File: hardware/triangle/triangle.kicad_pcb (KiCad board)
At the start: 4 copper layers, 100 x 86.6 mm, 70 parts, among them J1 USB_C_Receptacle_USB2.0_16P, J2 USB_C_Receptacle_USB2.0_16P, U2 EA8212HT6R

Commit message: rearranging shared files and input board beginnings
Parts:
- D1, D10, D11, D12, D13, D14, D15, D16, D17, D18, D19, D2, D20, D21, D22, D23, D24, D3, D4, D5, D6, D7, D8, D9: footprint footprints:LED_WS2812B-2020_PLCC4_2.0x2.0mm - no silkscreen -> easyeda2kicad:LED_WS2812B-2020_PLCC4_2.0x2.0mm - no silkscreen
- J1, J2: footprint footprints:TYPE-C-SMD_USB4120-03-C -> easyeda2kicad:TYPE-C-SMD_USB4120-03-C
- U2: footprint footprints:SOT-23-6_L2.9-W1.6-P0.95-LS2.8-BR -> easyeda2kicad:SOT-23-6_L2.9-W1.6-P0.95-LS2.8-BR
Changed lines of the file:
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@@
 		(embedded_fonts no)
 	)
-	(footprint "footprints:LED_WS2812B-2020_PLCC4_2.0x2.0mm - no silkscreen"
+	(footprint "easyeda2kicad:LED_WS2812B-2020_PLCC4_2.0x2.0mm - no silkscreen"
 		(layer "F.Cu")
 		(at 150 145 180)
@@
 		)
 	)
-	(footprint "footprints:LED_WS2812B-2020_PLCC4_2.0x2.0mm - no silkscreen"
+	(footprint "easyeda2kicad:LED_WS2812B-2020_PLCC4_2.0x2.0mm - no silkscreen"
 		(layer "F.Cu")
 		(at 165.5025 100.248125 -60)
@@
 		)
 	)
-	(footprint "footprints:LED_WS2812B-2020_PLCC4_2.0x2.0mm - no silkscreen"
+	(footprint "easyeda2kicad:LED_WS2812B-2020_PLCC4_2.0x2.0mm - no silkscreen"
 		(layer "F.Cu")
 		(at 189.02 143.84 -120)
@@
 		)
 	)
-	(footprint "footprints:LED_WS2812B-2020_PLCC4_2.0x2.0mm - no silkscreen"
+	(footprint "easyeda2kicad:LED_WS2812B-2020_PLCC4_2.0x2.0mm - no silkscreen"
 		(layer "F.Cu")
 		(at 118.995 127.09925 60)
@@
 		)
 	)
-	(footprint "footprints:LED_WS2812B-2020_PLCC4_2.0x2.0mm - no silkscreen"
+	(footprint "easyeda2kicad:LED_WS2812B-2020_PLCC4_2.0x2.0mm - no silkscreen"
 		(layer "F.Cu")
 		(at 160.335 145 180)
@@
 		)
 	)
-	(footprint "footprints:LED_WS2812B-2020_PLCC4_2.0x2.0mm - no silkscreen"
+	(footprint "easyeda2kicad:LED_WS2812B-2020_PLCC4_2.0x2.0mm - no silkscreen"
 		(layer "F.Cu")
 		(at 124.1625 118.148875 60)
@@
 		)
 	)
-	(footprint "footprints:LED_WS2812B-2020_PLCC4_2.0x2.0mm - no silkscreen"
+	(footprint "easyeda2kicad:LED_WS2812B-2020_PLCC4_2.0x2.0mm - no silkscreen"
 		(layer "F.Cu")
 		(at 186.1725 136.049625 -60)
@@
 		)
 	)
-	(footprint "footprints:LED_WS2812B-2020_PLCC4_2.0x2.0mm - no silkscreen"
+	(footprint "easyeda2kicad:LED_WS2812B-2020_PLCC4_2.0x2.0mm - no silkscreen"
 		(layer "F.Cu")
 		(at 139.665 91.29775 60)
@@
 		)
 	)
-	(footprint "footprints:LED_WS2812B-2020_PLCC4_2.0x2.0mm - no silkscreen"
+	(footprint "easyeda2kicad:LED_WS2812B-2020_PLCC4_2.0x2.0mm - no silkscreen"
 		(layer "F.Cu")
 		(at 134.4975 100.248125 60)
@@
 		)
 	)
-	(footprint "footprints:LED_WS2812B-2020_PLCC4_2.0x2.0mm - no silkscreen"
+	(footprint "easyeda2kicad:LED_WS2812B-2020_PLCC4_2.0x2.0mm - no silkscreen"
 		(layer "F.Cu")
 		(at 160.335 91.29775 -60)
@@
 		)
 	)
-	(footprint "footprints:LED_WS2812B-2020_PLCC4_2.0x2.0mm - no silkscreen"
+	(footprint "easyeda2kicad:LED_WS2812B-2020_PLCC4_2.0x2.0mm - no silkscreen"
 		(layer "F.Cu")
 		(at 144.8325 82.347375 60)
@@
 		)
 	)
-	(footprint "footprints:LED_WS2812B-2020_PLCC4_2.0x2.0mm - no silkscreen"
+	(footprint "easyeda2kicad:LED_WS2812B-2020_PLCC4_2.0x2.0mm - no silkscreen"
 		(layer "F.Cu")
 		(at 129.329999 145 180)
@@
 		(embedded_fonts no)
 	)
-	(footprint "footprints:LED_WS2812B-2020_PLCC4_2.0x2.0mm - no silkscreen"
+	(footprint "easyeda2kicad:LED_WS2812B-2020_PLCC4_2.0x2.0mm - no silkscreen"
 		(layer "F.Cu")
 		(at 110.825639 143.598161 120)
@@
 		)
 	)
-	(footprint "footprints:LED_WS2812B-2020_PLCC4_2.0x2.0mm - no silkscreen"
+	(footprint "easyeda2kicad:LED_WS2812B-2020_PLCC4_2.0x2.0mm - no silkscreen"
 		(layer "F.Cu")
 		(at 175.8375 118.148875 -60)
@@
 		)
 	)
-	(footprint "footprints:LED_WS2812B-2020_PLCC4_2.0x2.0mm - no silkscreen"
+	(footprint "easyeda2kicad:LED_WS2812B-2020_PLCC4_2.0x2.0mm - no silkscreen"
 		(layer "F.Cu")
 		(at 181.005 145 180)
@@
 		)
 	)
-	(footprint "footprints:LED_WS2812B-2020_PLCC4_2.0x2.0mm - no silkscreen"
+	(footprint "easyeda2kicad:LED_WS2812B-2020_PLCC4_2.0x2.0mm - no silkscreen"
 		(layer "F.Cu")
 		(at 170.67 145 180)
@@
 		)
 	)
-	(footprint "footprints:LED_WS2812B-2020_PLCC4_2.0x2.0mm - no silkscreen"
+	(footprint "easyeda2kicad:LED_WS2812B-2020_PLCC4_2.0x2.0mm - no silkscreen"
 		(layer "F.Cu")
 		(at 129.329999 109.1985 60)
@@
 		)
 	)
-	(footprint "footprints:LED_WS2812B-2020_PLCC4_2.0x2.0mm - no silkscreen"
+	(footprint "easyeda2kicad:LED_WS2812B-2020_PLCC4_2.0x2.0mm - no silkscreen"
 		(layer "F.Cu")
 		(at 113.8275 136.049625 60)
@@
 		(embedded_fonts no)
 	)
-	(footprint "footprints:LED_WS2812B-2020_PLCC4_2.0x2.0mm - no silkscreen"
+	(footprint "easyeda2kicad:LED_WS2812B-2020_PLCC4_2.0x2.0mm - no silkscreen"
 		(layer "F.Cu")
 		(at 170.67 109.1985 -60)
@@
 		)
 	)
-	(footprint "footprints:LED_WS2812B-2020_PLCC4_2.0x2.0mm - no silkscreen"
+	(footprint "easyeda2kicad:LED_WS2812B-2020_PLCC4_2.0x2.0mm - no silkscreen"
 		(layer "F.Cu")
 		(at 155.1675 82.347375 -60)
@@
 		)
 	)
-	(footprint "footprints:LED_WS2812B-2020_PLCC4_2.0x2.0mm - no silkscreen"
+	(footprint "easyeda2kicad:LED_WS2812B-2020_PLCC4_2.0x2.0mm - no silkscreen"
 		(layer "F.Cu")
 		(at 181.005 127.09925 -60)
@@
 		)
 	)
-	(footprint "footprints:LED_WS2812B-2020_PLCC4_2.0x2.0mm - no silkscreen"
+	(footprint "easyeda2kicad:LED_WS2812B-2020_PLCC4_2.0x2.0mm - no silkscreen"
 		(layer "F.Cu")
 		(at 118.995 145 180)
@@
 		)
 	)
-	(footprint "footprints:LED_WS2812B-2020_PLCC4_2.0x2.0mm - no silkscreen"
+	(footprint "easyeda2kicad:LED_WS2812B-2020_PLCC4_2.0x2.0mm - no silkscreen"
 		(layer "F.Cu")
 		(at 150 75.397)
@@
 		)
 	)
-	(footprint "footprints:LED_WS2812B-2020_PLCC4_2.0x2.0mm - no silkscreen"
+	(footprint "easyeda2kicad:LED_WS2812B-2020_PLCC4_2.0x2.0mm - no silkscreen"
 		(layer "F.Cu")
 		(at 139.665 145 180)
@@
 		)
 	)
-	(footprint "footprints:TYPE-C-SMD_USB4120-03-C"
+	(footprint "easyeda2kicad:TYPE-C-SMD_USB4120-03-C"
 		(layer "B.Cu")
 		(at 133.345625 130.607088 -150)
@@
 		)
 	)
-	(footprint "footprints:TYPE-C-SMD_USB4120-03-C"
+	(footprint "easyeda2kicad:TYPE-C-SMD_USB4120-03-C"
 		(layer "B.Cu")
 		(at 149.896593 102.269695 90)
@@
 		)
 	)
-	(footprint "footprints:SOT-23-6_L2.9-W1.6-P0.95-LS2.8-BR"
+	(footprint "easyeda2kicad:SOT-23-6_L2.9-W1.6-P0.95-LS2.8-BR"
 		(layer "B.Cu")
 		(at 165.576901 117.879661 30)
@@
 		)
 		(embedded_fonts no)
-		(model "${EASYEDA2KICAD}/easyeda2kicad.3dshapes/SOT-23-6_L2.9-W1.6-H1.5-LS2.8-P0.95.wrl"
+		(model "${KIPRJMOD}/../shared/easyeda2kicad.3dshapes/SOT-23-6_L2.9-W1.6-H1.5-LS2.8-P0.95.wrl"
 			(offset
 				(xyz 0 0 0)

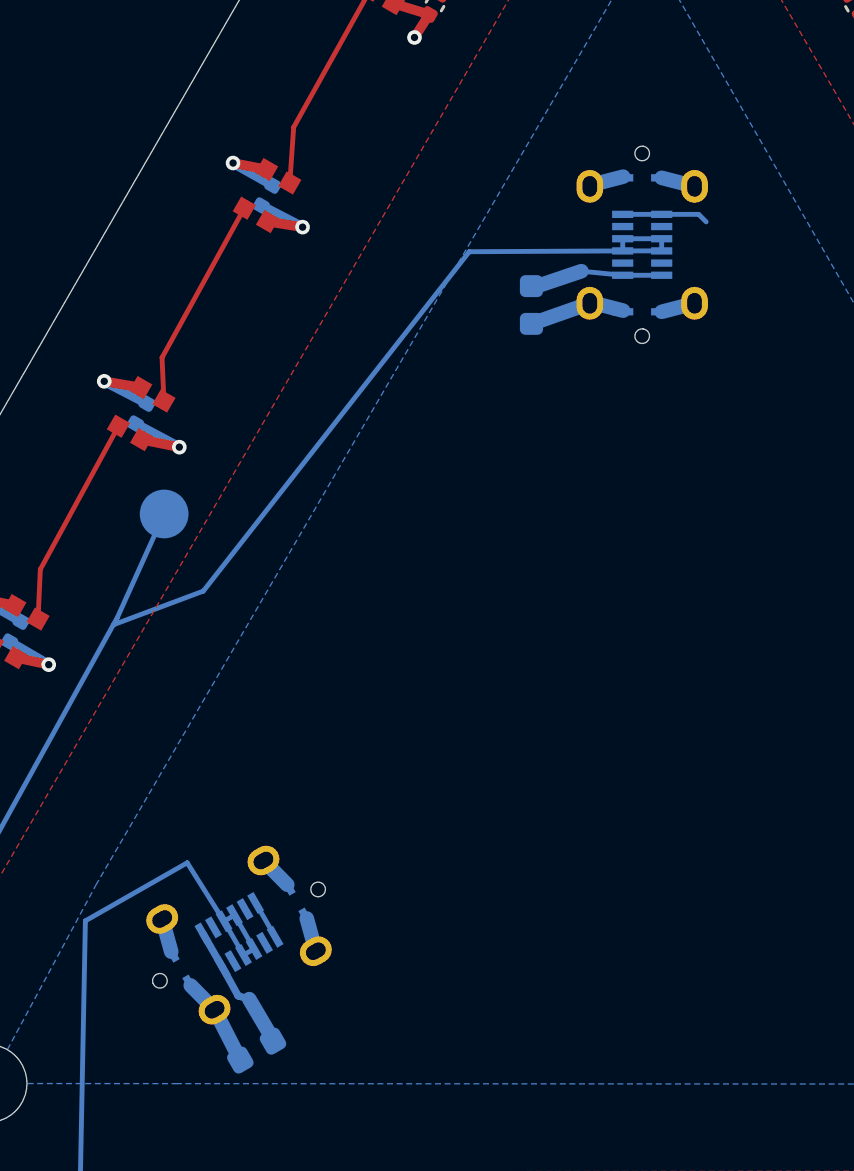
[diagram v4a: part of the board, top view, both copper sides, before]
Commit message: triangle rework to use new symbols and get all shapes
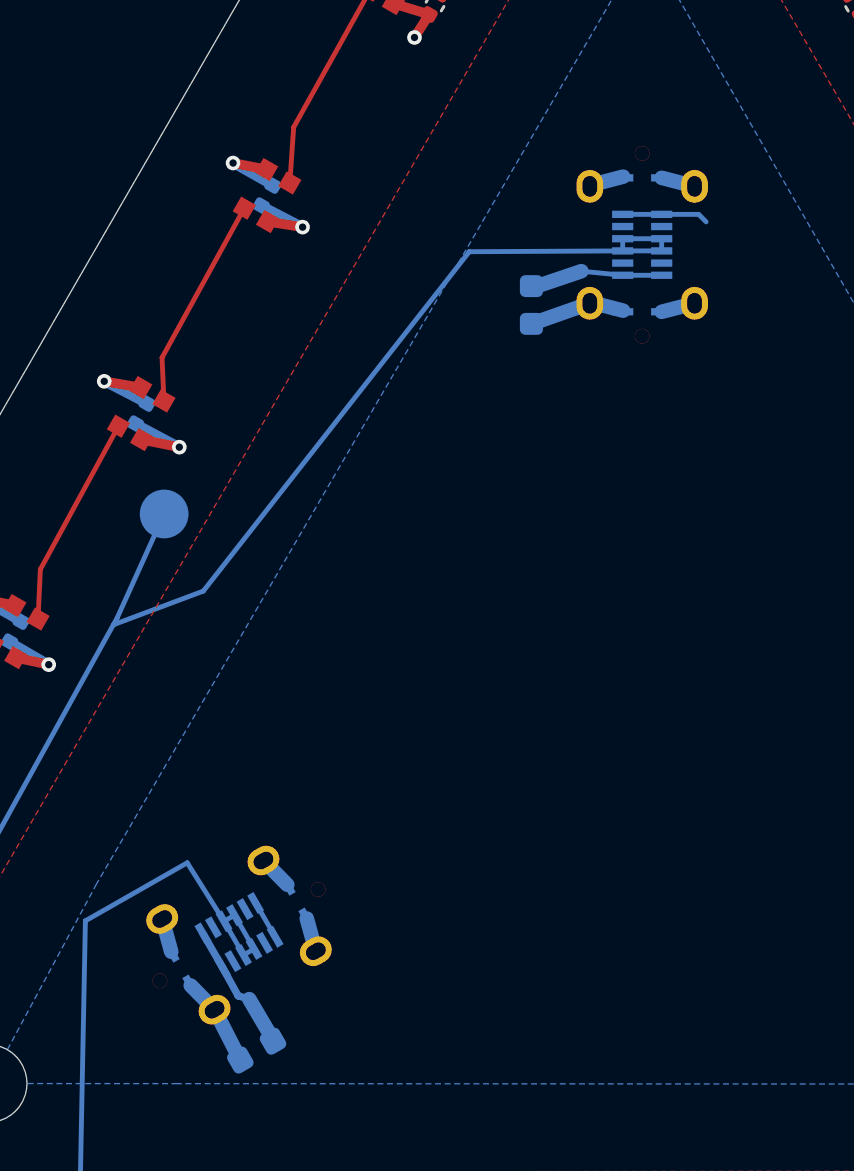
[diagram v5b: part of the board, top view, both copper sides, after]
